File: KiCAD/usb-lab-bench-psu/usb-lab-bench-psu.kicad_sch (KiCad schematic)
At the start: 12 parts, among them J1 Conn_02x02_Top_Bottom, J10 Conn_01x04, J11 Conn_01x04, J12 Conn_01x02, J2 Conn_01x04, J3 Conn_01x04, J4 Conn_01x02, J5 Conn_01x02, J6 Conn_01x04, J7 Conn_01x04, J8 Conn_01x04, J9 Conn_01x04

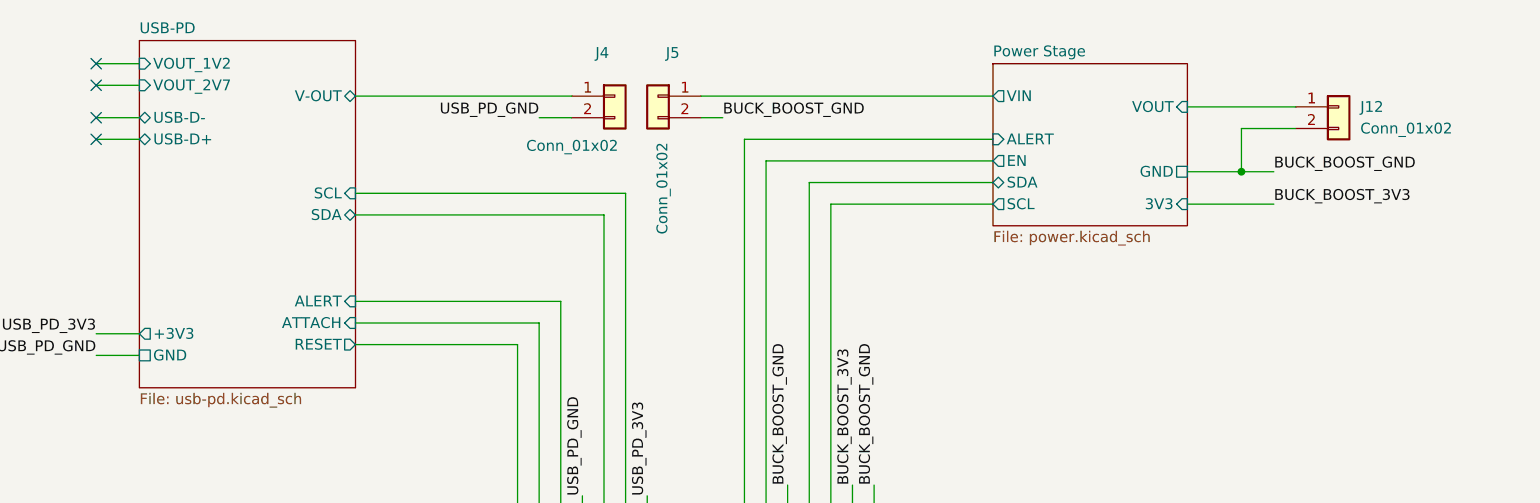
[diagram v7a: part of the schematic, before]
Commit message: Fixed label directions
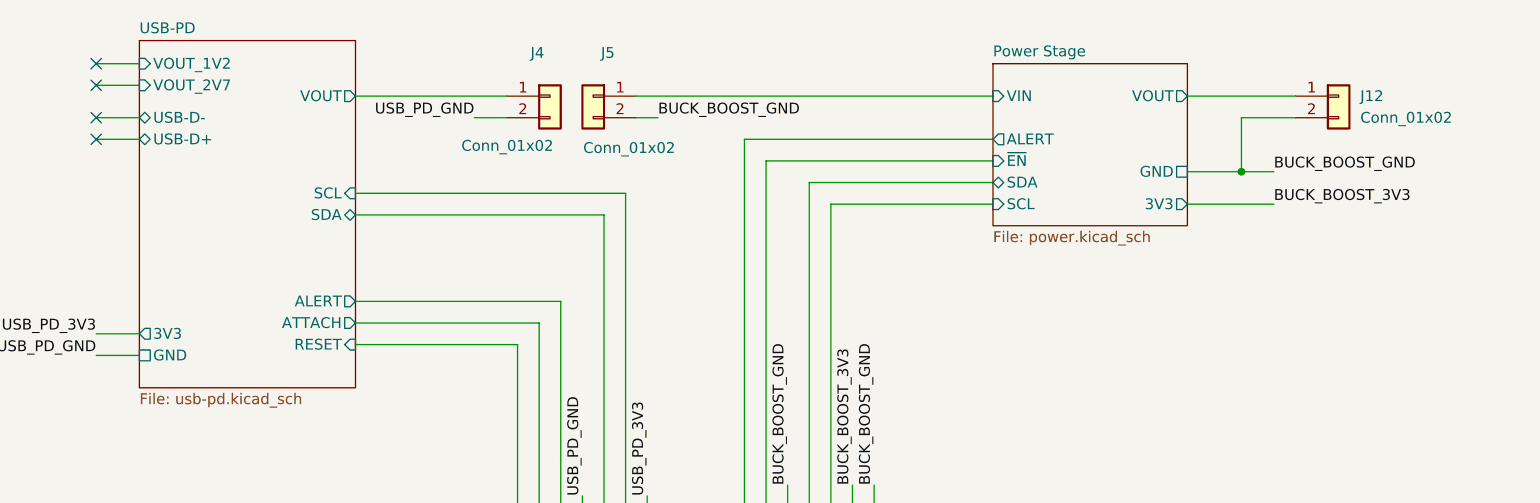
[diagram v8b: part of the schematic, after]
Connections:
- net Power Stage/EN renamed Power Stage/~{EN}
- net USB-PD/V-OUT renamed USB-PD/VOUT
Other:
- sheet Power Stage ports: added ~{EN}; removed EN
- sheet USB-PD ports: added 3V3, VOUT; removed +3V3, V-OUT
- moved on the sheet: J12, J4, J5
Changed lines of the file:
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@@
 	(wire
 		(pts
-			(xy 115.57 31.75) (xy 118.11 31.75)
+			(xy 107.95 31.75) (xy 110.49 31.75)
 		)
 		(stroke
@@
 	(wire
 		(pts
-			(xy 115.57 29.21) (xy 149.86 29.21)
+			(xy 107.95 29.21) (xy 149.86 29.21)
 		)
 		(stroke
@@
 	(wire
 		(pts
-			(xy 172.72 30.48) (xy 185.42 30.48)
+			(xy 172.72 29.21) (xy 185.42 29.21)
 		)
 		(stroke
@@
 	(wire
 		(pts
-			(xy 185.42 33.02) (xy 179.07 33.02)
+			(xy 185.42 31.75) (xy 179.07 31.75)
 		)
 		(stroke
@@
 	(wire
 		(pts
-			(xy 74.93 29.21) (xy 100.33 29.21)
+			(xy 74.93 29.21) (xy 92.71 29.21)
 		)
 		(stroke
@@
 	(wire
 		(pts
-			(xy 96.52 31.75) (xy 100.33 31.75)
+			(xy 88.9 31.75) (xy 92.71 31.75)
 		)
 		(stroke
@@
 	(wire
 		(pts
-			(xy 179.07 33.02) (xy 179.07 38.1)
+			(xy 179.07 31.75) (xy 179.07 38.1)
 		)
 		(stroke
@@
 	)
 	(label "USB_PD_GND"
-		(at 96.52 31.75 180)
+		(at 88.9 31.75 180)
 		(effects
 			(font
@@
 	)
 	(label "BUCK_BOOST_GND"
-		(at 118.11 31.75 0)
+		(at 110.49 31.75 0)
 		(effects
 			(font
@@
 	(symbol
 		(lib_id "Connector_Generic:Conn_01x02")
-		(at 190.5 30.48 0)
+		(at 190.5 29.21 0)
 		(unit 1)
 		(exclude_from_sim no)
@@
 		(fields_autoplaced yes)
 		(property "Reference" "J12"
-			(at 193.04 30.4799 0)
+			(at 193.04 29.2099 0)
 			(effects
 				(font
@@
 		)
 		(property "Value" "Conn_01x02"
-			(at 193.04 33.0199 0)
+			(at 193.04 31.7499 0)
 			(effects
 				(font
@@
 		)
 		(property "Footprint" ""
-			(at 190.5 30.48 0)
+			(at 190.5 29.21 0)
 			(effects
 				(font
@@
 		)
 		(property "Datasheet" "~"
-			(at 190.5 30.48 0)
+			(at 190.5 29.21 0)
 			(effects
 				(font
@@
 		)
 		(property "Description" "Generic connector, single row, 01x02, script generated (kicad-library-utils/schlib/autogen/connector/)"
-			(at 190.5 30.48 0)
+			(at 190.5 29.21 0)
 			(effects
 				(font
@@
 	(symbol
 		(lib_id "Connector_Generic:Conn_01x02")
-		(at 110.49 29.21 0)
+		(at 102.87 29.21 0)
 		(mirror y)
 		(unit 1)
@@
 		(dnp no)
 		(property "Reference" "J5"
-			(at 113.03 24.13 0)
+			(at 105.41 24.13 0)
 			(effects
 				(font
@@
 		)
 		(property "Value" "Conn_01x02"
-			(at 110.998 45.466 90)
+			(at 112.522 35.306 0)
 			(effects
 				(font
@@
 		)
 		(property "Footprint" ""
-			(at 110.49 29.21 0)
+			(at 102.87 29.21 0)
 			(effects
 				(font
@@
 		)
 		(property "Datasheet" "~"
-			(at 110.49 29.21 0)
+			(at 102.87 29.21 0)
 			(effects
 				(font
@@
 		)
 		(property "Description" "Generic connector, single row, 01x02, script generated (kicad-library-utils/schlib/autogen/connector/)"
-			(at 110.49 29.21 0)
+			(at 102.87 29.21 0)
 			(effects
 				(font
@@
 	(symbol
 		(lib_id "Connector_Generic:Conn_01x02")
-		(at 105.41 29.21 0)
+		(at 97.79 29.21 0)
 		(unit 1)
 		(exclude_from_sim no)
@@
 		(dnp no)
 		(property "Reference" "J4"
-			(at 103.124 24.13 0)
+			(at 95.504 24.13 0)
 			(effects
 				(font
@@
 		)
 		(property "Value" "Conn_01x02"
-			(at 94.996 35.052 0)
+			(at 87.376 35.052 0)
 			(effects
 				(font
@@
 		)
 		(property "Footprint" ""
-			(at 105.41 29.21 0)
+			(at 97.79 29.21 0)
 			(effects
 				(font
@@
 		)
 		(property "Datasheet" "~"
-			(at 105.41 29.21 0)
+			(at 97.79 29.21 0)
 			(effects
 				(font
@@
 		)
 		(property "Description" "Generic connector, single row, 01x02, script generated (kicad-library-utils/schlib/autogen/connector/)"
-			(at 105.41 29.21 0)
+			(at 97.79 29.21 0)
 			(effects
 				(font
@@
 			)
 		)
-		(pin "3V3" input
+		(pin "3V3" output
 			(at 172.72 41.91 0)
 			(effects
@@
 			)
 		)
-		(pin "VOUT" input
-			(at 172.72 30.48 0)
+		(pin "VOUT" output
+			(at 172.72 29.21 0)
 			(effects
 				(font
@@
 			)
 		)
-		(pin "EN" output
+		(pin "~{EN}" input
 			(at 149.86 36.83 180)
 			(effects
@@
 			)
 		)
-		(pin "VIN" output
+		(pin "VIN" input
 			(at 149.86 29.21 180)
 			(effects
@@
 			)
 		)
-		(pin "SCL" output
+		(pin "SCL" input
 			(at 149.86 41.91 180)
 			(effects
@@
 			)
 		)
-		(pin "ALERT" input
+		(pin "ALERT" output
 			(at 149.86 34.29 180)
 			(effects
@@
 			)
 		)
-		(pin "ALERT" input
+		(pin "ALERT" output
 			(at 74.93 53.34 0)
 			(effects
@@
 			)
 		)
-		(pin "V-OUT" bidirectional
+		(pin "VOUT" output
 			(at 74.93 29.21 0)
 			(effects
@@
 			)
 		)
-		(pin "ATTACH" input
+		(pin "ATTACH" output
 			(at 74.93 55.88 0)
 			(effects
@@
 			)
 		)
-		(pin "+3V3" output
+		(pin "3V3" output
 			(at 49.53 57.15 180)
 			(effects
@@
 			)
 		)
-		(pin "RESET" output
+		(pin "RESET" input
 			(at 74.93 58.42 0)
 			(effects
